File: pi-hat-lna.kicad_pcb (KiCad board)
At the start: 4 copper layers, 65 x 56 mm, 109 parts, among them J1 USB_B_Mini, J3 DNF, J4 VAL**, J5 VAL**, J6 2x3 0.1" HEADER, J7 VAL**, J8 VAL**, J9 CONN_01X02, M1 2118706-2, M2 2118706-2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

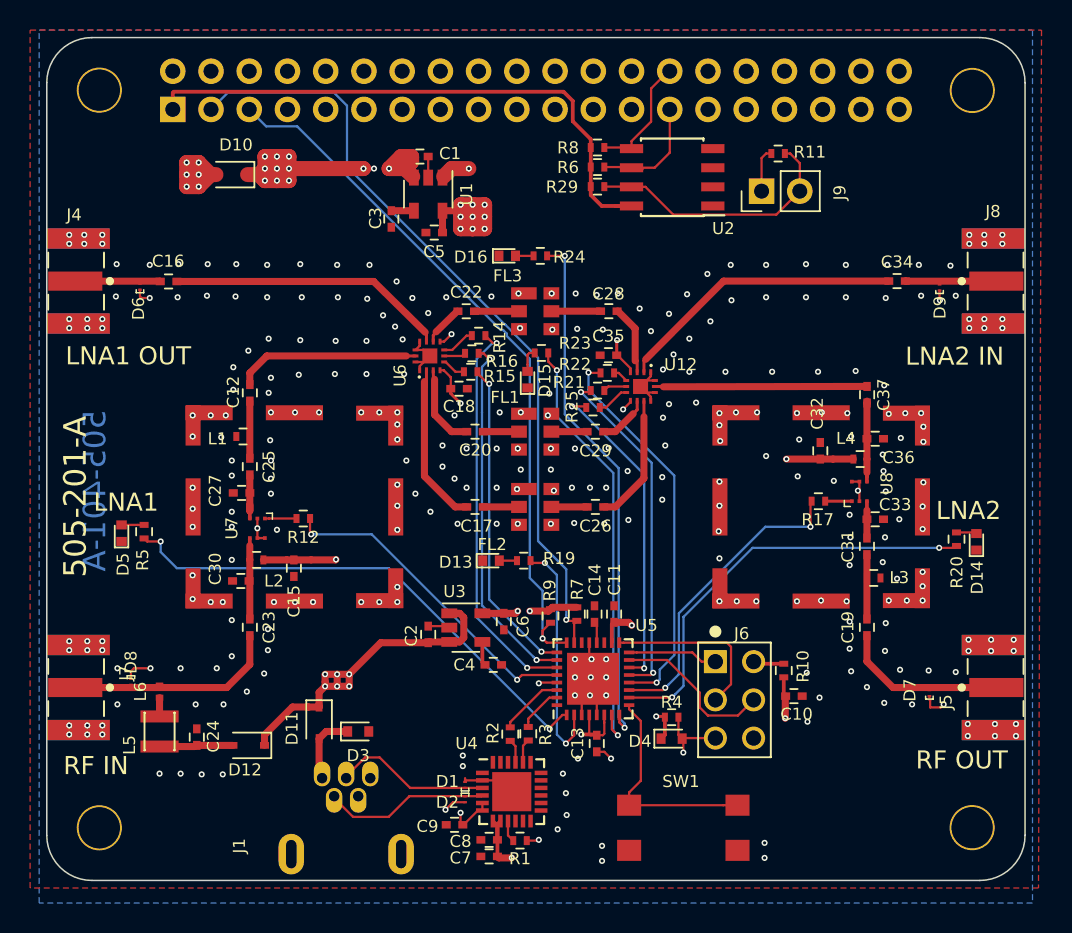
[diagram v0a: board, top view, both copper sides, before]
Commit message: Updated the I2C lines from the R-pi to connect to the appropriate pins on the ATMEGA328P:   SDA - pin 27 (PC4)   SCL - pin 28 (PC5) Also, updated the layout accordingly.
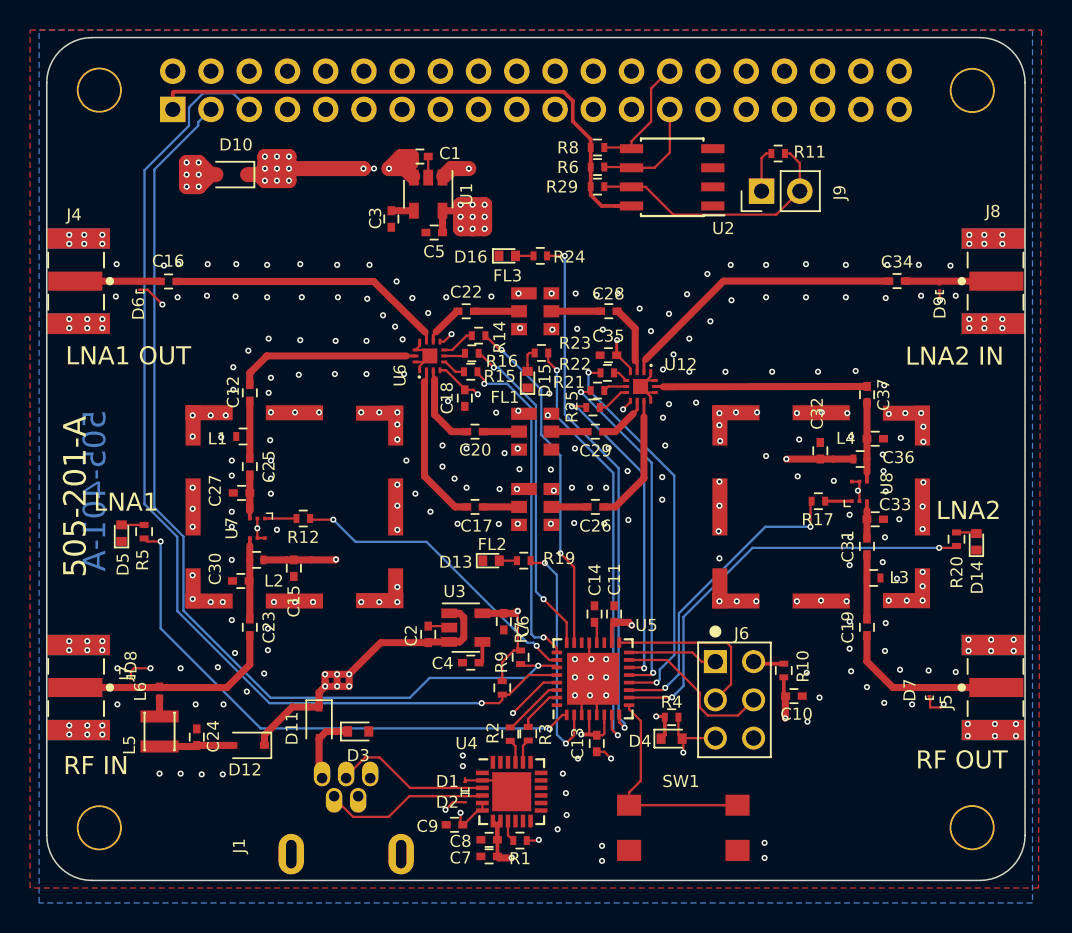
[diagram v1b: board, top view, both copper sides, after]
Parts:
- J4, J5, J7, J8: value VAL** -> SMA-J-P-H-ST-EM1
- M1, M2: value 2118706-2 -> DNF
- R11: value DNP -> DNF
- SW1: value VAL** -> TL3305AF160QG
- moved R9 5.75 mm to (108.8, 104.0)
- moved R7 4.71 mm to (110.0, 102.0)
- moved C4 1.50 mm to (106.7, 102.3), turned to 180 degrees
- moved C18 0.73 mm to (106.3, 84.8), turned to 90 degrees
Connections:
- U5 pad 23: /PI_SDA -> /avr-usb/SWA_V1
- U5 pad 24: /PI_SCL -> /avr-usb/SWA_V2
- U5 pad 26: /avr-usb/SWA_V2 -> /avr-usb/BYP_LNA2
- U5 pad 27: /avr-usb/SWA_V1 -> /PI_SDA
- U5 pad 28: /avr-usb/BYP_LNA2 -> /PI_SCL
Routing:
- net /PI_SCL: track 47.5 -> 69.2 mm
- net /PI_SDA: track 52.3 -> 65.0 mm
- net /avr-usb/SWA_V1: track 26.6 -> 22.9 mm
- net /avr-usb/LED1: track 34.2 -> 37.1 mm
- net +3V3: track 47.7 -> 50.1 mm, vias 6 -> 5
- net /avr-usb/SWA_V2: track 23.9 -> 21.9 mm
- net /avr-usb/BYP_LNA2: track 21.5 -> 20.4 mm
- net GND: track 35.9 -> 36.6 mm, vias 311 -> 310
- net /avr-usb/SWA_V3: track 21.5 -> 22.2 mm
